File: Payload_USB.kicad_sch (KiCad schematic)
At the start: 21 parts, among them IC1 USB2422T-I_MJ, J1 USB_A, J2 USB_A, J5 USB_B_Mini, J6 Conn_01x03, J7 Conn_01x03, U3 TPS2066CDGN, Y1 Crystal

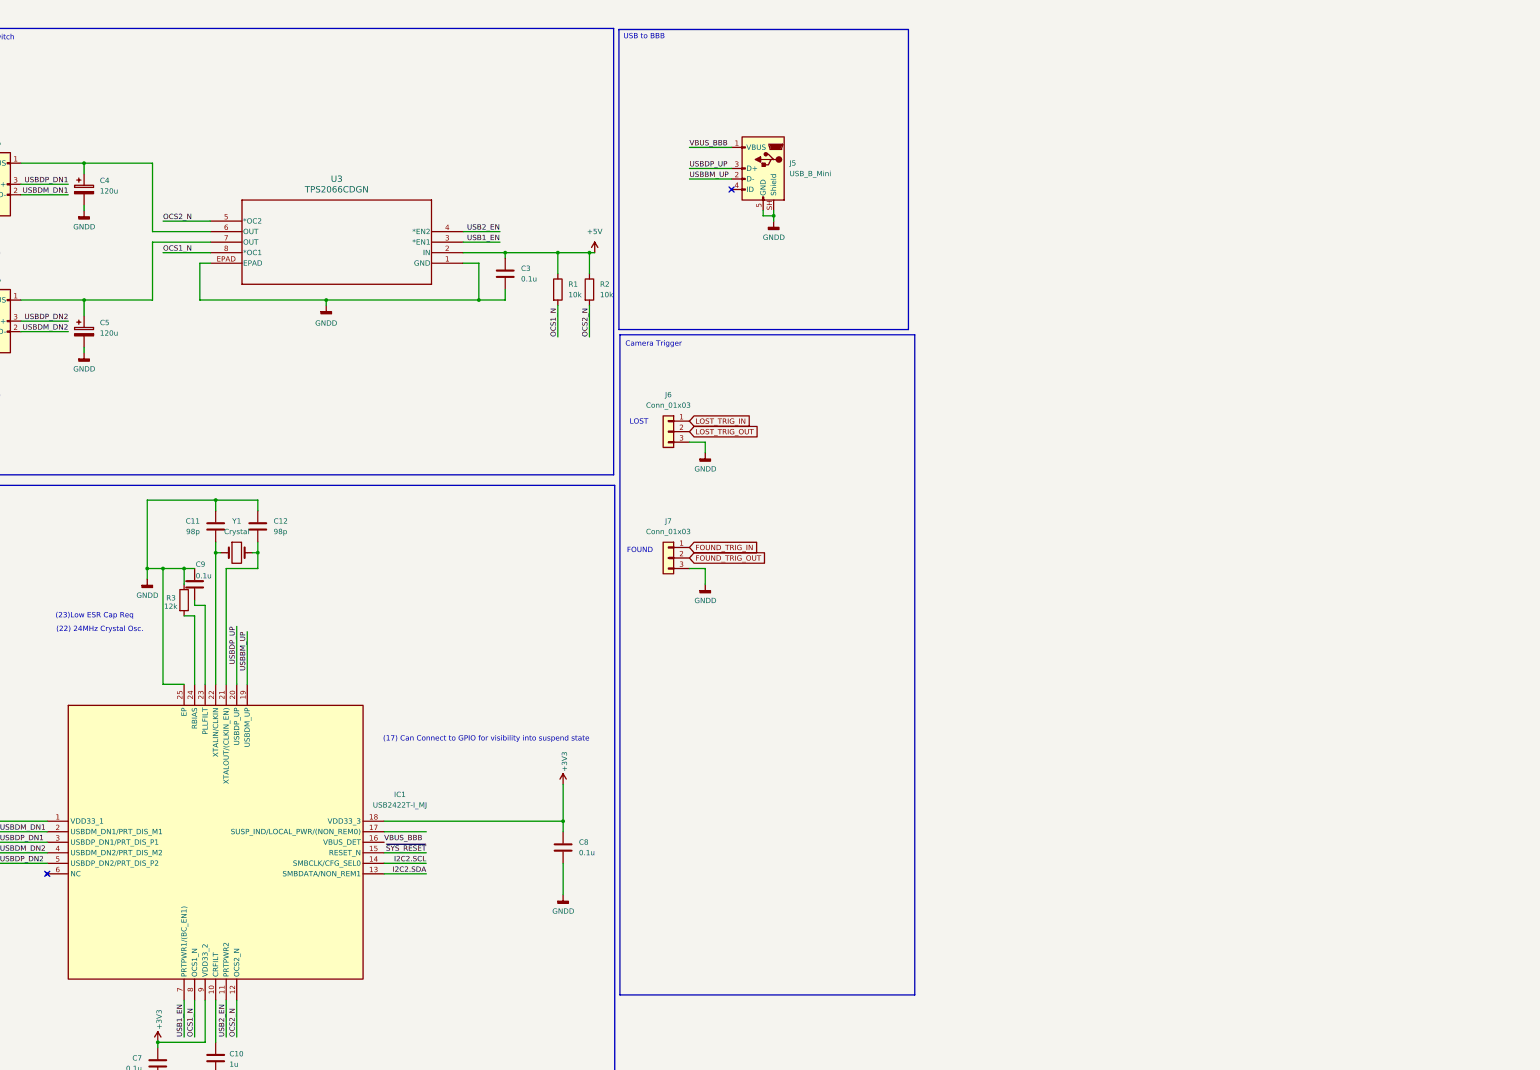
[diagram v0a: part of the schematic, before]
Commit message: Payload OVP, GNSS, Star Tracker Pinouts added
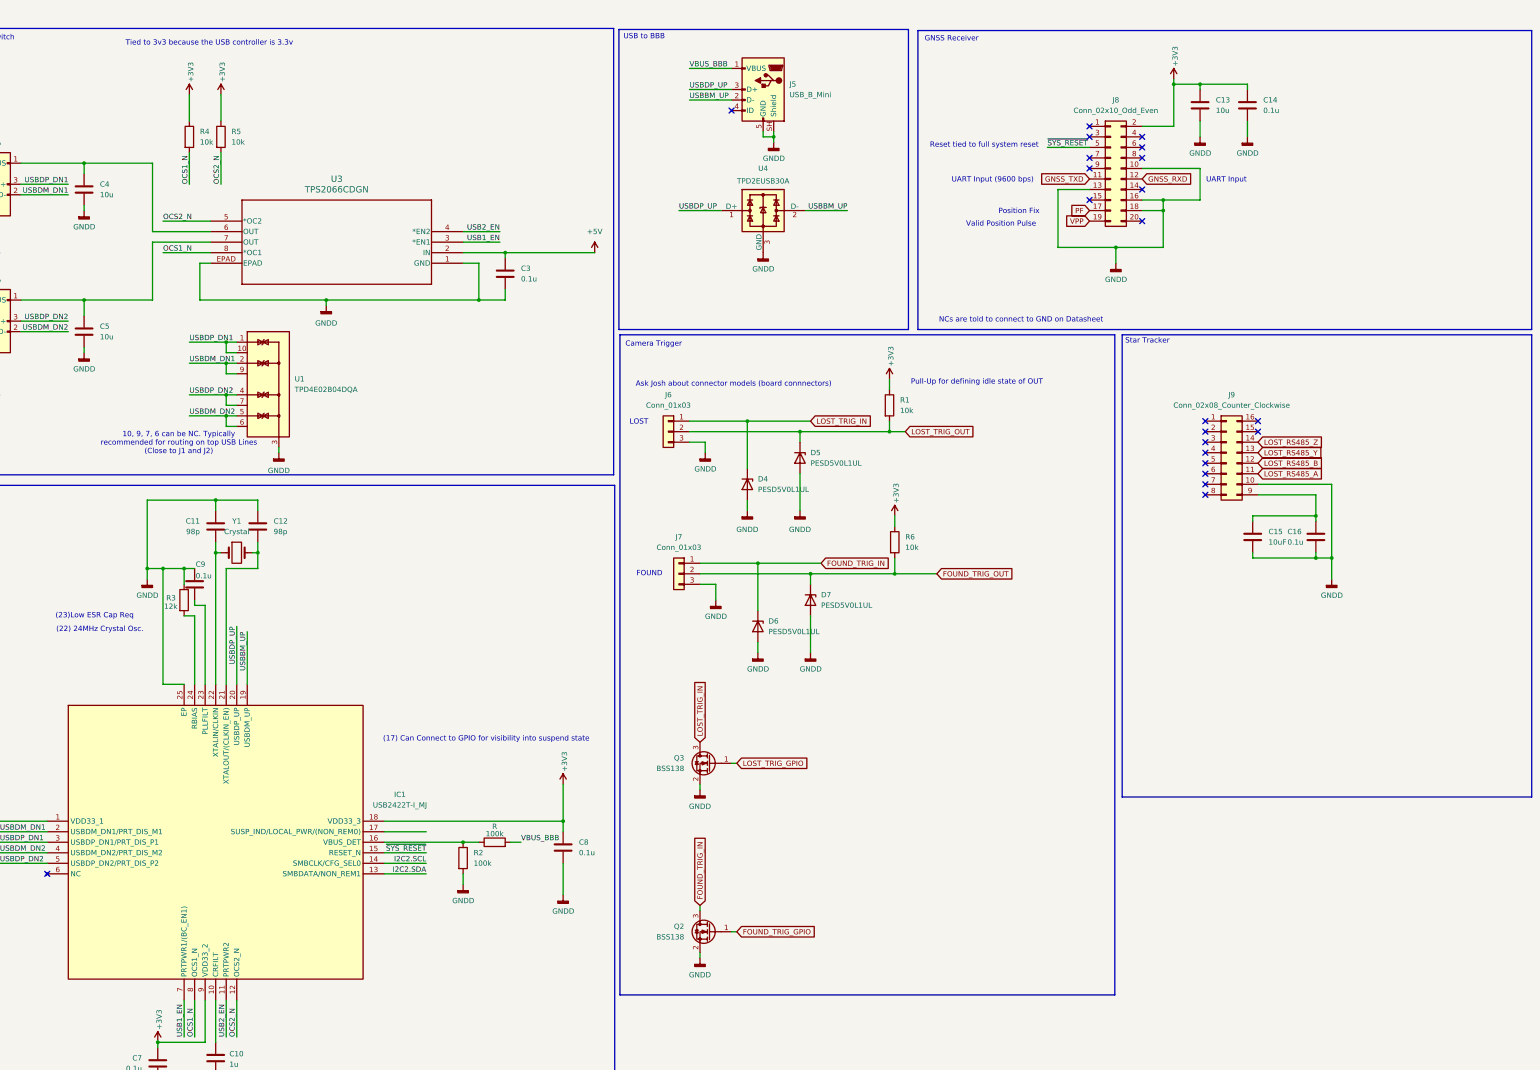
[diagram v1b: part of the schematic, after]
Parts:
- removed C4, C5: 120u, symbol Device:C_Polarized
- added C13, C4, C5: 10u, symbol Device:C
- added C14, C16: 0.1u, symbol Device:C
- added C15: 10uF, symbol Device:C
- added D4, D5, D6, D7: PESD5V0L1UL, Diode_SMD:D_SOD-882, symbol Diode:PESD5V0L1UL
- added J8: Conn_02x10_Odd_Even, symbol Connector_Generic:Conn_02x10_Odd_Even
- added J9: Conn_02x08_Counter_Clockwise, symbol Connector_Generic:Conn_02x08_Counter_Clockwise
- added Q2, Q3: BSS138, Package_TO_SOT_SMD:SOT-23, symbol Transistor_FET:BSS138
- added R: 100k, symbol Device:R
- added R4, R5, R6: 10k, symbol Device:R
- added U1: TPD4E02B04DQA, Package_SON:USON-10_2.5x1.0mm_P0.5mm, symbol Power_Protection:TPD4E02B04DQA
- added U4: TPD2EUSB30A, Package_TO_SOT_SMD:Texas_DRT-3, symbol Power_Protection:TPD2EUSB30A
- R2: value 10k -> 100k
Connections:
- net +3V3: now also R1.1, C13.1, C14.1, J8.2 (Pin_2), R4.1, R5.1, R6.1
- net +5V: no longer R1.1, R2.1
- net FOUND_TRIG_IN: now also D6.1 (K), Q2.3 (D)
- net FOUND_TRIG_OUT: now also D7.1 (K), R6.2
- net GNDD: now also R2.2, C13.2, C14.2, C15.2, C16.2, C4.2, C5.2, D4.2 (A), D5.2 (A), D6.2 (A), D7.2 (A), J8.10 (Pin_10), J8.13 (Pin_13), J8.16 (Pin_16), J8.18 (Pin_18), J9.10 (Pin_10), Q2.2 (S), Q3.2 (S), U1.3 (G), U1.8 (G), U4.3 (GND)
- net LOST_TRIG_IN: now also D4.1 (K), Q3.3 (D)
- net LOST_TRIG_OUT: now also R1.2, D5.1 (K)
- net OCS1_N: now also R4.2; no longer R1.2
- net OCS2_N: now also R5.2; no longer R2.2
- net USBBM_UP: now also U4.2 (D-)
- net USBDM_DN1: now also U1.2 (IO2), U1.9 (NC)
- net USBDM_DN2: now also U1.5 (IO4), U1.6 (NC)
- net USBDP_DN1: now also U1.1 (IO1), U1.10 (NC)
- net USBDP_DN2: now also U1.4 (IO3), U1.7 (NC)
- net USBDP_UP: now also U4.1 (D+)
- net VBUS_BBB: now also R.2; no longer IC1.16 (VBUS_DET)
- net ~{SYS_RESET}: now also J8.5 (Pin_5)
- net at J1.1 (VBUS), U3.6 (OUT): now also C4.1
- net at J2.1 (VBUS), U3.7 (OUT): now also C5.1
- new net: IC1.16 (VBUS_DET), R.1, R2.1
- new net: C15.1, C16.1, J9.9 (Pin_9)
- new net FOUND_TRIG_GPIO: Q2.1 (G)
- new net GNSS_RXD: J8.12 (Pin_12)
- new net GNSS_TXD: J8.11 (Pin_11)
- new net LOST_RS485_A: J9.11 (Pin_11)
- new net LOST_RS485_B: J9.12 (Pin_12)
- new net LOST_RS485_Y: J9.13 (Pin_13)
- new net LOST_RS485_Z: J9.14 (Pin_14)
- new net LOST_TRIG_GPIO: Q3.1 (G)
- new net PF: J8.17 (Pin_17)
- new net VPP: J8.19 (Pin_19)
- no-connect marks 2 -> 22
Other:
- note added: "10, 9, 7, 6 can be NC. Typically recommended for routing on top USB Lines (Close to J1 and J2)"
- note added: "Ask Josh about connector models (board connnectors)"
- note added: "GNSS Receiver"
- note added: "NCs are told to connect to GND on Datasheet"
- note added: "Position Fix"
- note added: "Pull-Up for defining idle state of OUT"
- note added: "Reset tied to full system reset"
- note added: "Star Tracker"
- note added: "Tied to 3v3 because the USB controller is 3.3v"
- note added: "UART Input"
- note added: "UART Input (9600 bps)"
- note added: "Valid Position Pulse"
- moved on the sheet: J5, J7

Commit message: Payload USB updated to have 4 USB 2.0 Hub
Added support for USB flash or eUSB flash for storage.
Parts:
- removed C10: 1u, symbol Device:C
- removed C11, C12: 98p, symbol Device:C
- removed C6, C7, C8, C9: 0.1u, symbol Device:C
- removed IC1: USB2422T-I_MJ, QFN50P400X400X100-25N-D, symbol HS2_CDH:USB2422T-I_MJ
- removed R, R2: 100k, symbol Device:R
- removed R3: 12k, symbol Device:R
- removed Y1: Crystal, symbol Device:Crystal
- added C17, C18: 22p, symbol Device:C
- added C19, C20, C25: 1u, symbol Device:C
- added C21, C23, C24, C26, C27, C28, C29, C30: 0.1u, symbol Device:C
- added C22: 10u, symbol Device:C
- added FB2: FerriteBead, symbol Device:FerriteBead
- added J11: USB_A, symbol Connector:USB_A
- added R16, R17: 100k, symbol Device:R
- added R18: 10k, symbol Device:R
- added R19: 12k, symbol Device:R
- added U5: USB2514B_Bi, Package_DFN_QFN:QFN-36-1EP_6x6mm_P0.5mm_EP3.7x3.7mm, symbol Interface_USB:USB2514B_Bi
- added U6: TPS2066CDGN, HS2-CDH:DGN8_1P89x1P57_TEX, symbol HS2_CDH:TPS2066CDGN
- added U7: TPD2EUSB30A, Package_TO_SOT_SMD:Texas_DRT-3, symbol Power_Protection:TPD2EUSB30A
- added Y3: Crystal_GND23, symbol Device:Crystal_GND23
- C15: value 10uF -> 10u
- J8: footprint (none) -> Connector_PinHeader_2.00mm:PinHeader_2x10_P2.00mm_Vertical
- U3: footprint DGN8_1P89x1P57_TEX -> HS2-CDH:DGN8_1P89x1P57_TEX
- renumbered C3 to C11, D4 to D2, D6 to D3, D5 to D4, D7 to D5, J1 to J3, J2 to J4, J6 to J5, J7 to J6, J5 to J7, Q3 to Q1, R1 to R12, R6 to R13, R4 to R8, R5 to R9, U1 to U2
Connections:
- net +3V3: now also C19.1, C23.1, C24.1, FB2.1, R18.1, U5.15 (VDD33), U5.23 (VDD33)
- net +5V: now also C21.1, U6.2 (IN)
- net GNDD: now also C17.1, C18.1, C19.2, C20.2, C21.2, C22.2, C23.2, C24.2, C25.2, C26.2, C27.2, C28.2, C29.2, C30.2, J11.4 (GND), J11.SH (Shield), R16.2, R19.2, U5.37 (VSS), U6.1 (GND), U6.EPAD, U7.3 (GND), Y3.2 (G), Y3.3 (G)
- net I2C2.SCL: now also U5.24 (SCL/SMBCLK/CFG_SEL0)
- net I2C2.SDA: now also U5.22 (SDA/SMBDATA/NON_REM1)
- net OCS1_N: now also U5.13 (OCS_N1)
- net OCS2_N: now also U5.17 (OCS_N2)
- net USB1_EN: now also U5.12 (PRTPWR1/BC_EN1), U5.16 (PRTPWR2/BC_EN2), U5.18 (PRTPWR3/BC_EN3)
- net USBBM_UP: now also U5.30 (USBDM_UP)
- net USBDM_DN1: now also U5.1 (USBDM_DN1/PRT_DIS_M1)
- net USBDM_DN2: now also U5.3 (USBDM_DN2/PRT_DIS_M2)
- net USBDP_DN1: now also U5.2 (USBDP_DN1/PRT_DIS_P1)
- net USBDP_DN2: now also U5.4 (USBDP_DN2/PRT_DIS_P2)
- net USBDP_UP: now also U5.31 (USBDP_UP)
- net VBUS_BBB: now also R17.2
- net ~{SYS_RESET}: now also U5.26 (RESET_N)
- new net: C20.1, C27.1, C28.1, C29.1, C30.1, FB2.2, U5.10 (VDDA33), U5.29 (VDDA33), U5.36 (VDDA33), U5.5 (VDDA33)
- new net: R16.1, R17.1, U5.27 (VBUS_DET)
- new net: C18.2, U5.33 (XTALIN/CLKIN), Y3.4
- new net: C17.2, U5.32 (XTALOUT), Y3.1
- new net: R19.1, U5.35 (RBIAS)
- new net: C22.1, J11.1 (VBUS), U6.7 (OUT)
- new net: C25.1, U5.14 (CRFILT)
- new net: C26.1, U5.34 (PLLFILT)
- new net OCS3_N: R18.2, U5.19 (OCS_N3), U6.8 (*OC1)
- new net USB3_EN: U6.3 (*EN1)
- new net USBDM_DN3: J11.2 (D-), U5.6 (USBDM_DN3/PRT_DIS_M3), U7.2 (D-)
- new net USBDP_DN3: J11.3 (D+), U5.7 (USBDP_DN3/PRT_DIS_P3), U7.1 (D+)
- no-connect marks 22 -> 29
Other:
- note added: "(14,34)Low ESR Cap Req"
- note added: "(28) Can Connect to GPIO for visibility into suspend state"
- note added: "(32,33) 24MHz Crystal Osc."
- note added: "10, 9, 7, 6 can be NC. Typically recommended for routing on top USB Lines (Close to J3 and J4)"
- note added: "2 TPS2066 are used for current supplying capabilities and reverse blocking"
- note added: "Divider needed here"
- note added: "eUSB Flash"
- note removed: "(10) Low ESR Cap Req"
- note removed: "(17) Can Connect to GPIO for visibility into suspend state"
- note removed: "(22) 24MHz Crystal Osc."
- note removed: "(23)Low ESR Cap Req"
- note removed: "10, 9, 7, 6 can be NC. Typically recommended for routing on top USB Lines (Close to J1 and J2)"
- moved on the sheet: C11, C4, C5, J3, J4, R8, R9, U3

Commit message: Update
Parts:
- removed C16: 0.1u, symbol Device:C
- added C32: 0.1u, symbol Device:C
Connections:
- net +5V: now also C15.1, J9.2 (Pin_2), C32.1
- net GNDD: now also J9.1 (Pin_1), C32.2; no longer J9.10 (Pin_10)
- net LOST_RS485_A: now also J9.6 (Pin_6); no longer J9.11 (Pin_11)
- net LOST_RS485_B: now also J9.5 (Pin_5); no longer J9.12 (Pin_12)
- net LOST_RS485_Y: now also J9.3 (Pin_3); no longer J9.13 (Pin_13)
- net LOST_RS485_Z: now also J9.4 (Pin_4); no longer J9.14 (Pin_14)
- net at J9.9 (Pin_9): no longer C15.1
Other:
- moved on the sheet: J9
